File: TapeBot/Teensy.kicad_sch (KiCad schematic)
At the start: 1 part, among them U1 Teensy4.1

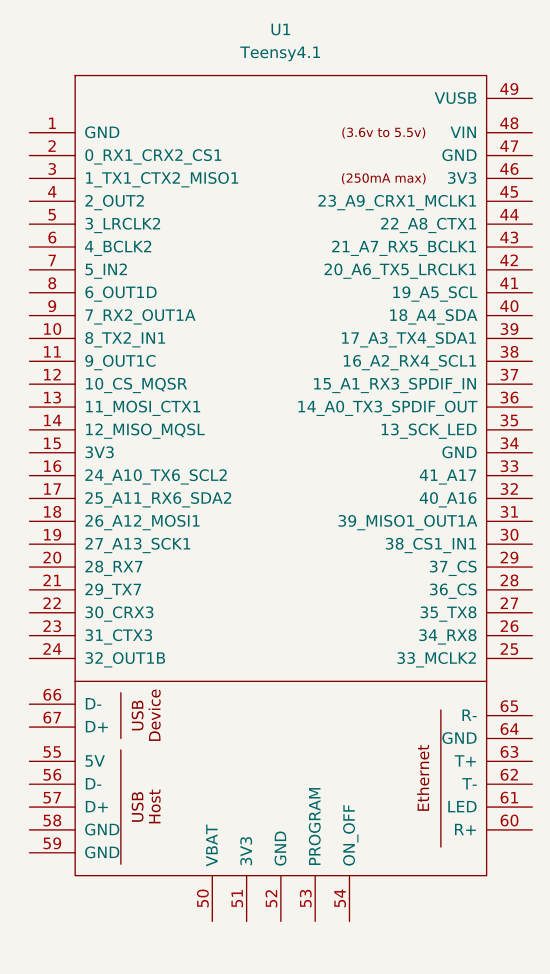
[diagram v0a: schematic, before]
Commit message: fixed footprints and symbols
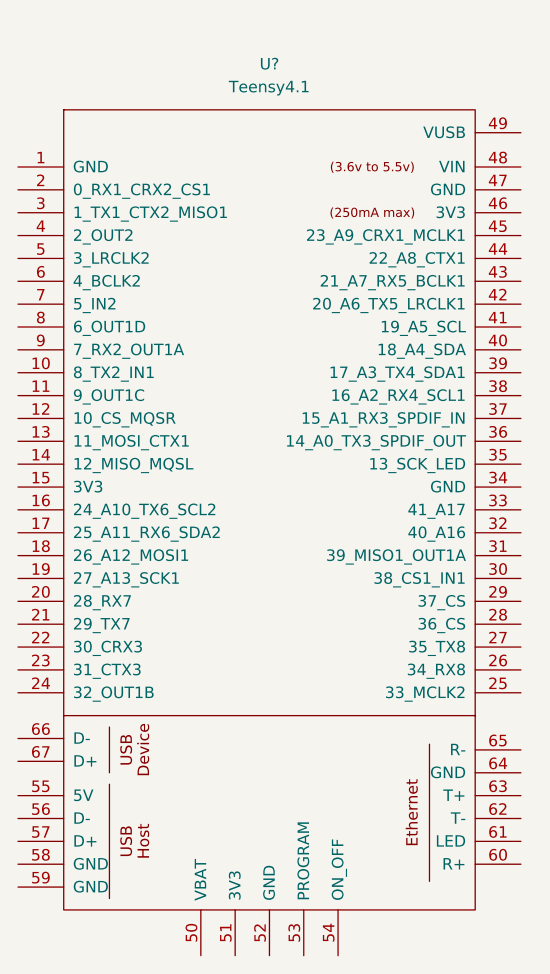
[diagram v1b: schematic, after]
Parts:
- removed U1: Teensy4.1, symbol teensy:Teensy4.1
- added U?: Teensy4.1, teensy:Teensy41, symbol teensy:Teensy4.1
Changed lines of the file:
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@@
     )
   )
-  (symbol (lib_id "teensy:Teensy4.1") (at 146.05 102.87 0) (unit 1)
+  (symbol (lib_id "teensy:Teensy4.1") (at 144.78 106.68 0) (unit 1)
     (in_bom yes) (on_board yes) (fields_autoplaced)
-    (property "Reference" "U1" (id 0) (at 146.05 36.83 0))
-    (property "Value" "Teensy4.1" (id 1) (at 146.05 39.37 0))
-    (property "Footprint" "" (id 2) (at 135.89 92.71 0)
+    (property "Reference" "U?" (id 0) (at 144.78 40.64 0))
+    (property "Value" "Teensy4.1" (id 1) (at 144.78 43.18 0))
+    (property "Footprint" "teensy:Teensy41" (id 2) (at 134.62 96.52 0)
       (effects (font (size 1.27 1.27)) hide)
     )
-    (property "Datasheet" "" (id 3) (at 135.89 92.71 0)
+    (property "Datasheet" "" (id 3) (at 134.62 96.52 0)
       (effects (font (size 1.27 1.27)) hide)
     )

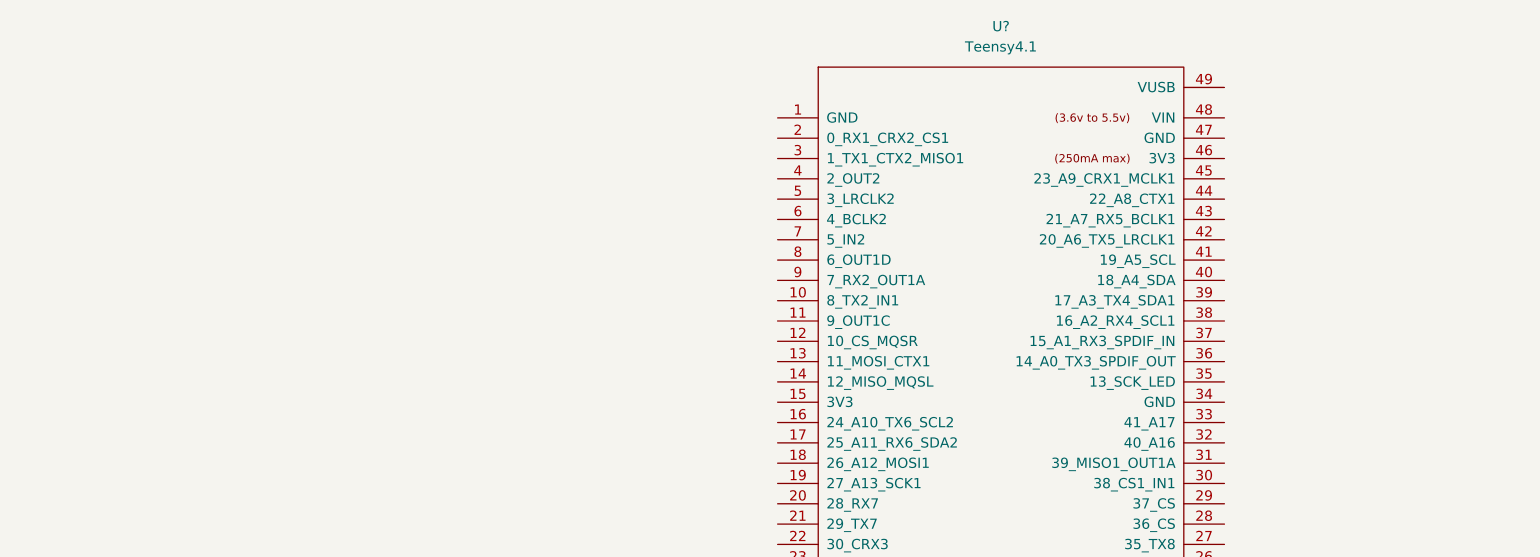
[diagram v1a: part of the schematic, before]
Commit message: finished motor driver schematic and load cell schematic
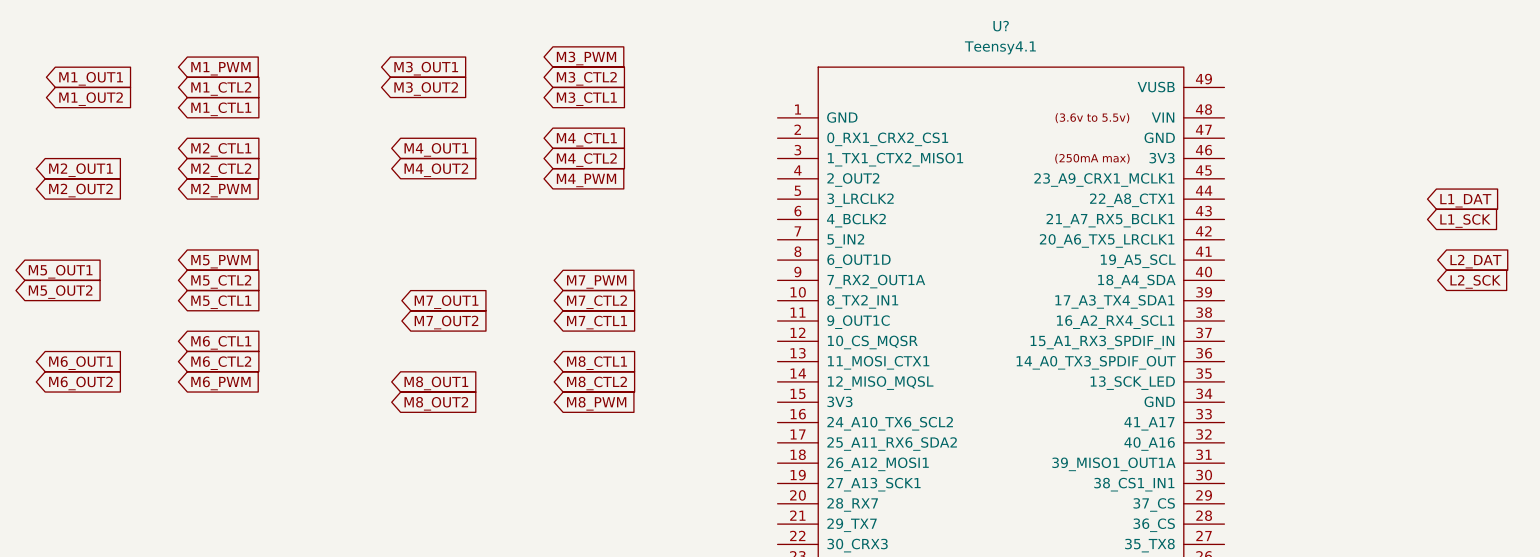
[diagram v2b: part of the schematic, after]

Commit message: added label
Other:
- note added: "Teensy 4.1"
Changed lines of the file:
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@@
     )
+  )
+  (text "Teensy 4.1\n" (at 24.13 24.13 0)
+    (effects (font (size 3 3) (thickness 1) bold) (justify left bottom))
   )
   (global_label "M6_CTL2" (shape input) (at 41.91 82.55 0) (fields_autoplaced)

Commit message: (mostly) finished schematic
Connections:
- net L1_DAT: now also U?.32 (40_A16)
- net L1_SCK: now also U?.33 (41_A17)
- net L2_DAT: now also U?.38 (16_A2_RX4_SCL1)
- net L2_SCK: now also U?.16 (24_A10_TX6_SCL2)
- net M1_CTL1: now also U?.11 (9_OUT1C)
- net M1_CTL2: now also U?.10 (8_TX2_IN1)
- net M1_OUT1: now also U?.4 (2_OUT2)
- net M1_OUT2: now also U?.3 (1_TX1_CTX2_MISO1)
- net M1_PWM: now also U?.9 (7_RX2_OUT1A)
- net M2_CTL1: now also U?.40 (18_A4_SDA)
- net M2_CTL2: now also U?.39 (17_A3_TX4_SDA1)
- net M2_OUT1: now also U?.36 (14_A0_TX3_SPDIF_OUT)
- net M2_OUT2: now also U?.37 (15_A1_RX3_SPDIF_IN)
- net M2_PWM: now also U?.41 (19_A5_SCL)
- net M3_CTL1: now also U?.7 (5_IN2)
- net M3_CTL2: now also U?.6 (4_BCLK2)
- net M3_OUT1: now also U?.44 (22_A8_CTX1)
- net M3_OUT2: now also U?.45 (23_A9_CRX1_MCLK1)
- net M3_PWM: now also U?.8 (6_OUT1D)
- net M4_CTL1: now also U?.13 (11_MOSI_CTX1)
- net M4_CTL2: now also U?.14 (12_MISO_MQSL)
- net M4_OUT1: now also U?.43 (21_A7_RX5_BCLK1)
- net M4_OUT2: now also U?.42 (20_A6_TX5_LRCLK1)
- net M4_PWM: now also U?.12 (10_CS_MQSR)
- net M5_CTL1: now also U?.20 (28_RX7)
- net M5_CTL2: now also U?.19 (27_A13_SCK1)
- net M5_OUT1: now also U?.18 (26_A12_MOSI1)
- net M5_OUT2: now also U?.17 (25_A11_RX6_SDA2)
- net M5_PWM: now also U?.21 (29_TX7)
- net M6_CTL1: now also U?.30 (38_CS1_IN1)
- net M6_CTL2: now also U?.31 (39_MISO1_OUT1A)
- net M6_PWM: now also U?.29 (37_CS)
- net M7_CTL1: now also U?.27 (35_TX8)
- net M7_CTL2: now also U?.26 (34_RX8)
- net M7_PWM: now also U?.28 (36_CS)

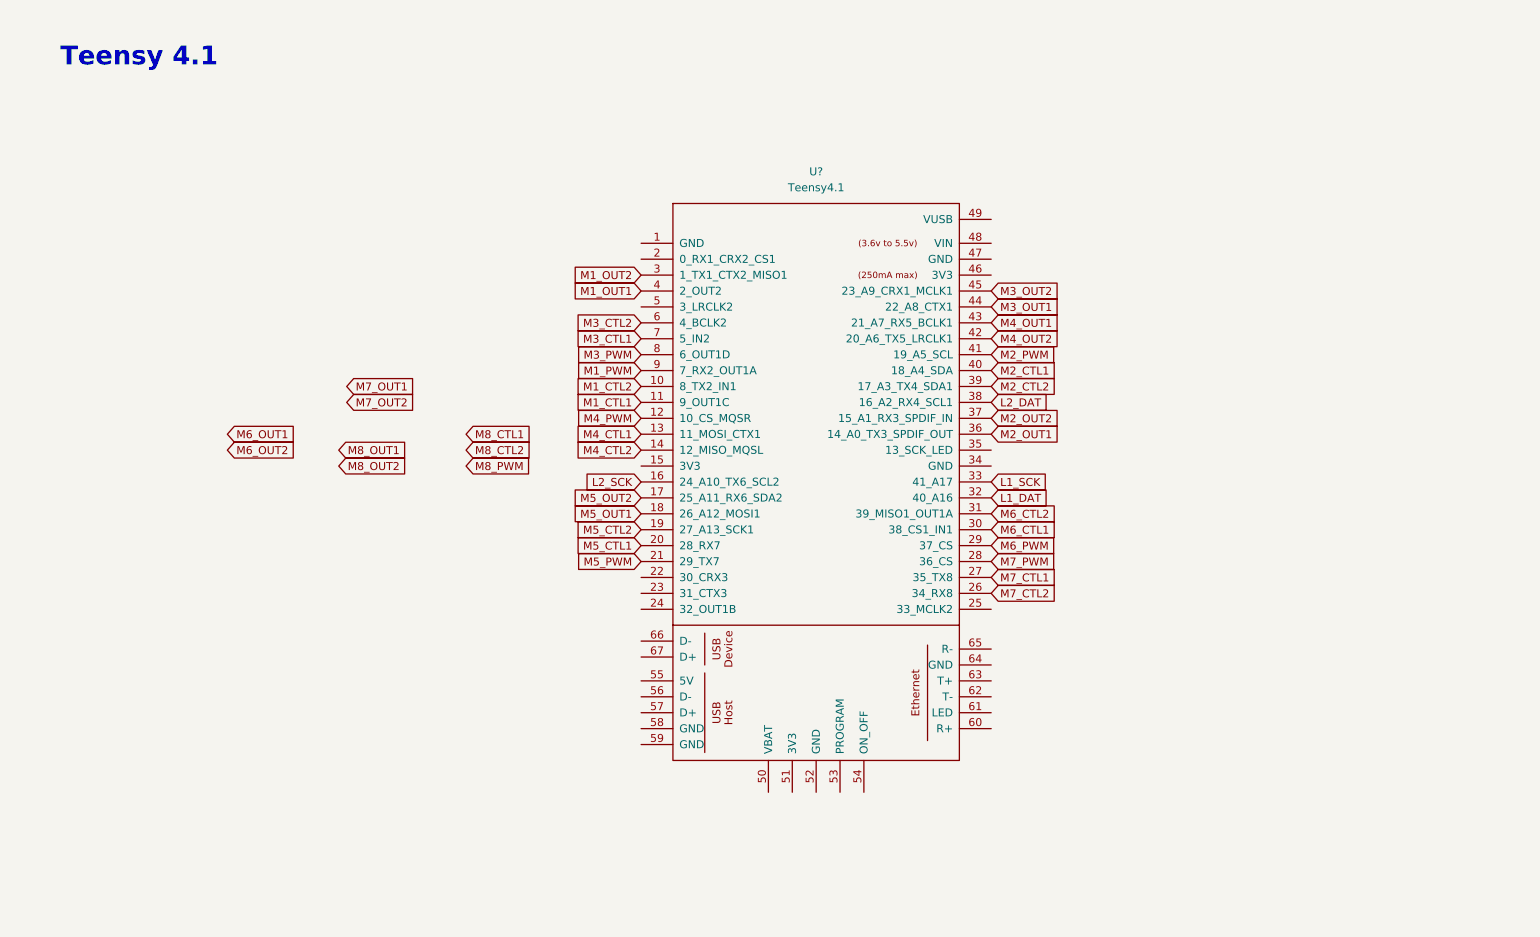
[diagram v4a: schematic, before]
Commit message: fixed footprints and 3d models
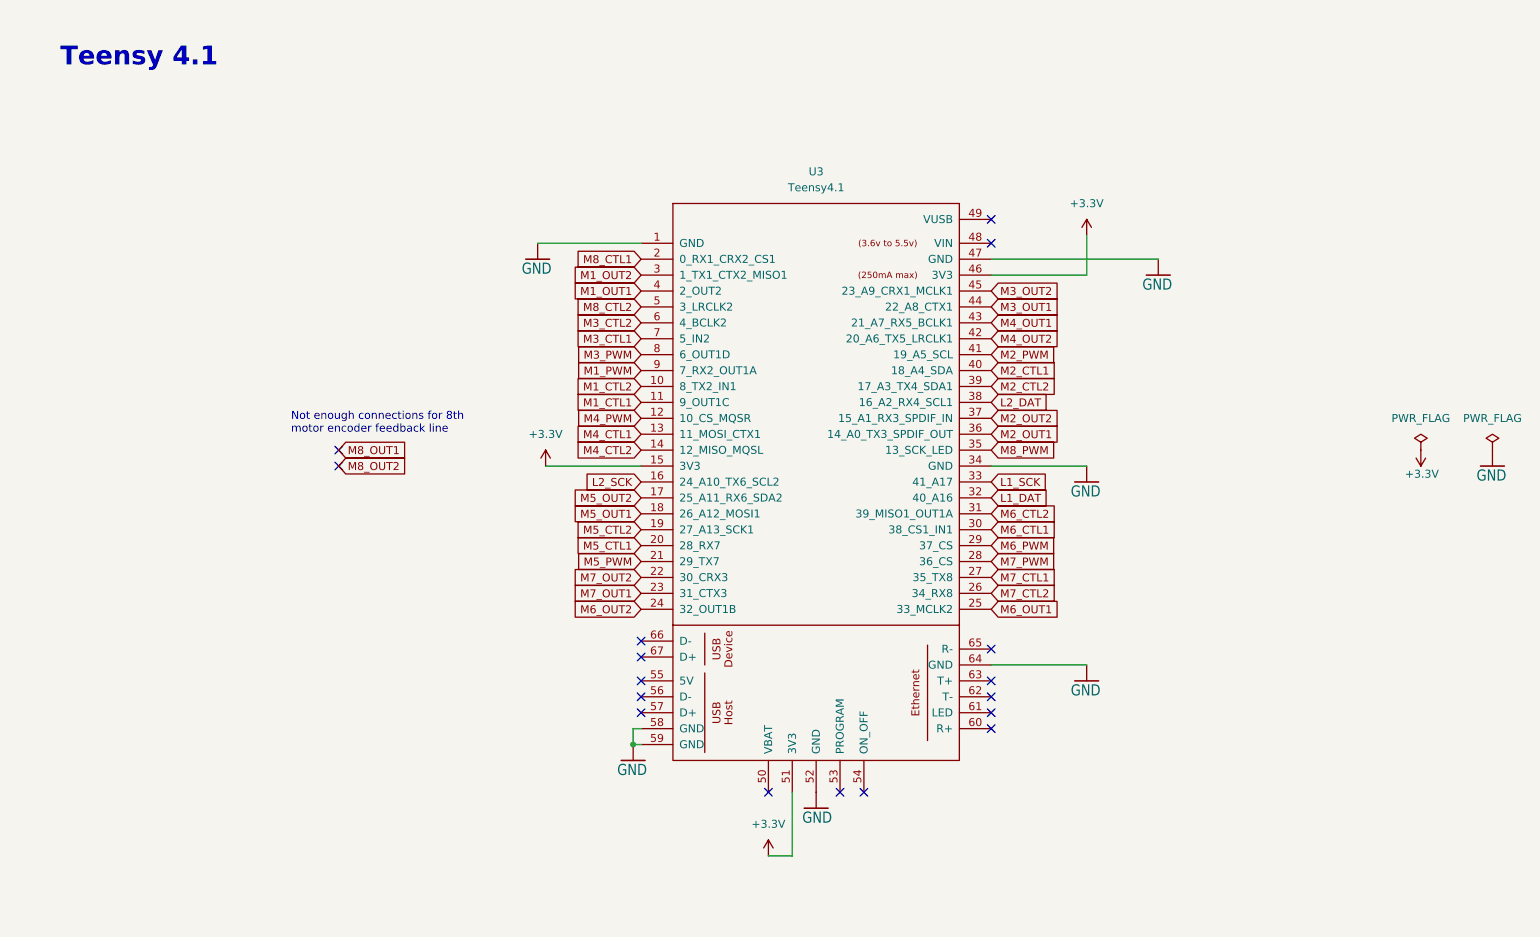
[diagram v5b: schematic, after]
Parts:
- gave numbers to parts that had none: 1
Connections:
- net M6_OUT1: now also U3.25 (33_MCLK2)
- net M6_OUT2: now also U3.24 (32_OUT1B)
- net M7_OUT1: now also U3.23 (31_CTX3)
- net M7_OUT2: now also U3.22 (30_CRX3)
- net M8_CTL1: now also U3.2 (0_RX1_CRX2_CS1)
- net M8_CTL2: now also U3.5 (3_LRCLK2)
- net M8_PWM: now also U3.35 (13_SCK_LED)
- net GND: now reaches U3.1 (GND)
- net GND: now also U3.34 (GND), U3.47 (GND), U3.52 (GND), U3.58 (GND), U3.59 (GND), U3.64 (GND)
- net +3.3V: now reaches U3.15 (3V3)
- net +3.3V: now also U3.46 (3V3), U3.51 (3V3)
- no-connect marks 0 -> 17
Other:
- note added: "Not enough connections for 8th motor encoder feedback line"

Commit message: arranged board
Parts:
- added H1, H2, H3, H4: MountingHole_Pad, MountingHole:MountingHole_4.3mm_M4_DIN965_Pad, symbol Mechanical:MountingHole_Pad
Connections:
- net GND: now also H1.1, H2.1, H3.1, H4.1
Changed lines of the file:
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@@
     (company "CHARM LAB")
   )
+  (junction (at 220.98 154.94) (diameter 0) (color 0 0 0 0)
+  )
+  (junction (at 220.98 147.32) (diameter 0) (color 0 0 0 0)
+  )
   (junction (at 115.57 132.08) (diameter 0) (color 0 0 0 0)
   )
+  (junction (at 220.98 139.7) (diameter 0) (color 0 0 0 0)
+  )
   (no_connect (at 116.84 121.92))
   (no_connect (at 116.84 124.46))
@@
   (no_connect (at 68.58 85.09))
   (no_connect (at 68.58 87.63))
+  (wire (pts (xy 220.98 139.7) (xy 220.98 147.32))
+    (stroke (width 0) (type default) (color 0 0 0 0))
+  )
   (wire (pts (xy 172.72 87.63) (xy 187.96 87.63))
     (stroke (width 0) (type default) (color 0 0 0 0))
   )
+  (wire (pts (xy 220.98 132.08) (xy 220.98 139.7))
+    (stroke (width 0) (type default) (color 0 0 0 0))
+  )
   (wire (pts (xy 187.96 50.8) (xy 187.96 57.15))
     (stroke (width 0) (type default) (color 0 0 0 0))
@@
     (stroke (width 0) (type default) (color 0 0 0 0))
   )
+  (wire (pts (xy 220.98 147.32) (xy 220.98 154.94))
+    (stroke (width 0) (type default) (color 0 0 0 0))
+  )
   (wire (pts (xy 115.57 132.08) (xy 116.84 132.08))
     (stroke (width 0) (type default) (color 0 0 0 0))
@@
   (symbol (lib_id "power:+3.3V") (at 241.3 85.09 180) (unit 1)
     (in_bom yes) (on_board yes)
-    (property "Reference" "#PWR0101" (id 0) (at 241.3 81.28 0)
+    (property "Reference" "#PWR018" (id 0) (at 241.3 81.28 0)
       (effects (font (size 1.27 1.27)) hide)
     )
@@
   (symbol (lib_id "power:PWR_FLAG") (at 252.73 85.09 0) (unit 1)
     (in_bom yes) (on_board yes) (fields_autoplaced)
-    (property "Reference" "#FLG0102" (id 0) (at 252.73 83.185 0)
+    (property "Reference" "#FLG02" (id 0) (at 252.73 83.185 0)
       (effects (font (size 1.27 1.27)) hide)
     )
@@
     (pin "1")
   )
+  (symbol (lib_name "MountingHole_Pad_1") (lib_id "Mechanical:MountingHole_Pad") (at 223.52 132.08 270) (unit 1)
+    (in_bom yes) (on_board yes) (fields_autoplaced)
+    (property "Reference" "H1" (id 0) (at 227.33 130.8099 90)
+      (effects (font (size 1.27 1.27)) (justify left))
+    )
+    (property "Value" "MountingHole_Pad" (id 1) (at 227.33 133.3499 90)
+      (effects (font (size 1.27 1.27)) (justify left))
+    )
+    (property "Footprint" "MountingHole:MountingHole_4.3mm_M4_DIN965_Pad" (id 2) (at 223.52 132.08 0)
+      (effects (font (size 1.27 1.27)) hide)
+    )
+    (property "Datasheet" "~" (id 3) (at 223.52 132.08 0)
+      (effects (font (size 1.27 1.27)) hide)
+    )
+    (pin "1")
+  )
   (symbol (lib_id "SparkFun_Motor_Driver-TB6612FNG_v11c-eagle-import:GND") (at 252.73 87.63 0) (unit 1)
     (in_bom yes) (on_board yes)
-    (property "Reference" "#GND0101" (id 0) (at 252.73 87.63 0)
+    (property "Reference" "#GND026" (id 0) (at 252.73 87.63 0)
       (effects (font (size 1.27 1.27)) hide)
     )
@@
     (pin "1")
   )
+  (symbol (lib_name "MountingHole_Pad_2") (lib_id "Mechanical:MountingHole_Pad") (at 223.52 139.7 270) (unit 1)
+    (in_bom yes) (on_board yes) (fields_autoplaced)
+    (property "Reference" "H2" (id 0) (at 227.33 138.4299 90)
+      (effects (font (size 1.27 1.27)) (justify left))
+    )
+    (property "Value" "MountingHole_Pad" (id 1) (at 227.33 140.9699 90)
+      (effects (font (size 1.27 1.27)) (justify left))
+    )
+    (property "Footprint" "MountingHole:MountingHole_4.3mm_M4_DIN965_Pad" (id 2) (at 223.52 139.7 0)
+      (effects (font (size 1.27 1.27)) hide)
+    )
+    (property "Datasheet" "~" (id 3) (at 223.52 139.7 0)
+      (effects (font (size 1.27 1.27)) hide)
+    )
+    (pin "1")
+  )
+  (symbol (lib_id "SparkFun_Motor_Driver-TB6612FNG_v11c-eagle-import:GND") (at 220.98 157.48 0) (unit 1)
+    (in_bom yes) (on_board yes)
+    (property "Reference" "#GND025" (id 0) (at 220.98 157.48 0)
+      (effects (font (size 1.27 1.27)) hide)
+    )
+    (property "Value" "GND" (id 1) (at 218.44 160.02 0)
+      (effects (font (size 1.778 1.5113)) (justify left bottom))
+    )
+    (property "Footprint" "SparkFun_Motor_Driver-TB6612FNG_v11c:" (id 2) (at 220.98 157.48 0)
+      (effects (font (size 1.27 1.27)) hide)
+    )
+    (property "Datasheet" "" (id 3) (at 220.98 157.48 0)
+      (effects (font (size 1.27 1.27)) hide)
+    )
+    (pin "1")
+  )
   (symbol (lib_id "power:+3.3V") (at 101.6 87.63 0) (unit 1)
     (in_bom yes) (on_board yes) (fields_autoplaced)
@@
   (symbol (lib_id "power:PWR_FLAG") (at 241.3 85.09 0) (unit 1)
     (in_bom yes) (on_board yes) (fields_autoplaced)
-    (property "Reference" "#FLG0101" (id 0) (at 241.3 83.185 0)
+    (property "Reference" "#FLG01" (id 0) (at 241.3 83.185 0)
       (effects (font (size 1.27 1.27)) hide)
     )
@@
       (effects (font (size 1.27 1.27)) hide)
     )
+    (pin "1")
+  )
+  (symbol (lib_name "MountingHole_Pad_3") (lib_id "Mechanical:MountingHole_Pad") (at 223.52 147.32 270) (unit 1)
+    (in_bom yes) (on_board yes) (fields_autoplaced)
+    (property "Reference" "H3" (id 0) (at 227.33 146.0499 90)
+      (effects (font (size 1.27 1.27)) (justify left))
+    )
+    (property "Value" "MountingHole_Pad" (id 1) (at 227.33 148.5899 90)
+      (effects (font (size 1.27 1.27)) (justify left))
+    )
+    (property "Footprint" "MountingHole:MountingHole_4.3mm_M4_DIN965_Pad" (id 2) (at 223.52 147.32 0)
+      (effects (font (size 1.27 1.27)) hide)
+    )
+    (property "Datasheet" "~" (id 3) (at 223.52 147.32 0)
+      (effects (font (size 1.27 1.27)) hide)
+    )
+    (pin "1")
+  )
+  (symbol (lib_id "Mechanical:MountingHole_Pad") (at 223.52 154.94 270) (unit 1)
+    (in_bom yes) (on_board yes) (fields_autoplaced)
+    (property "Reference" "H4" (id 0) (at 227.33 153.6699 90)
+      (effects (font (size 1.27 1.27)) (justify left))
+    )
+    (property "Value" "MountingHole_Pad" (id 1) (at 227.33 156.2099 90)
+      (effects (font (size 1.27 1.27)) (justify left))
+    )
+    (property "Footprint" "MountingHole:MountingHole_4.3mm_M4_DIN965_Pad" (id 2) (at 223.52 154.94 0)
+      (effects (font (size 1.27 1.27)) hide)
+    )
+    (property "Datasheet" "~" (id 3) (at 223.52 154.94 0)
+      (effects (font (size 1.27 1.27)) hide)
+    )
